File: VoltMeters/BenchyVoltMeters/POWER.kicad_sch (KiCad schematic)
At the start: 25 parts, among them J1 POWER CONN, U10 AP3401, U9 TPS7A94

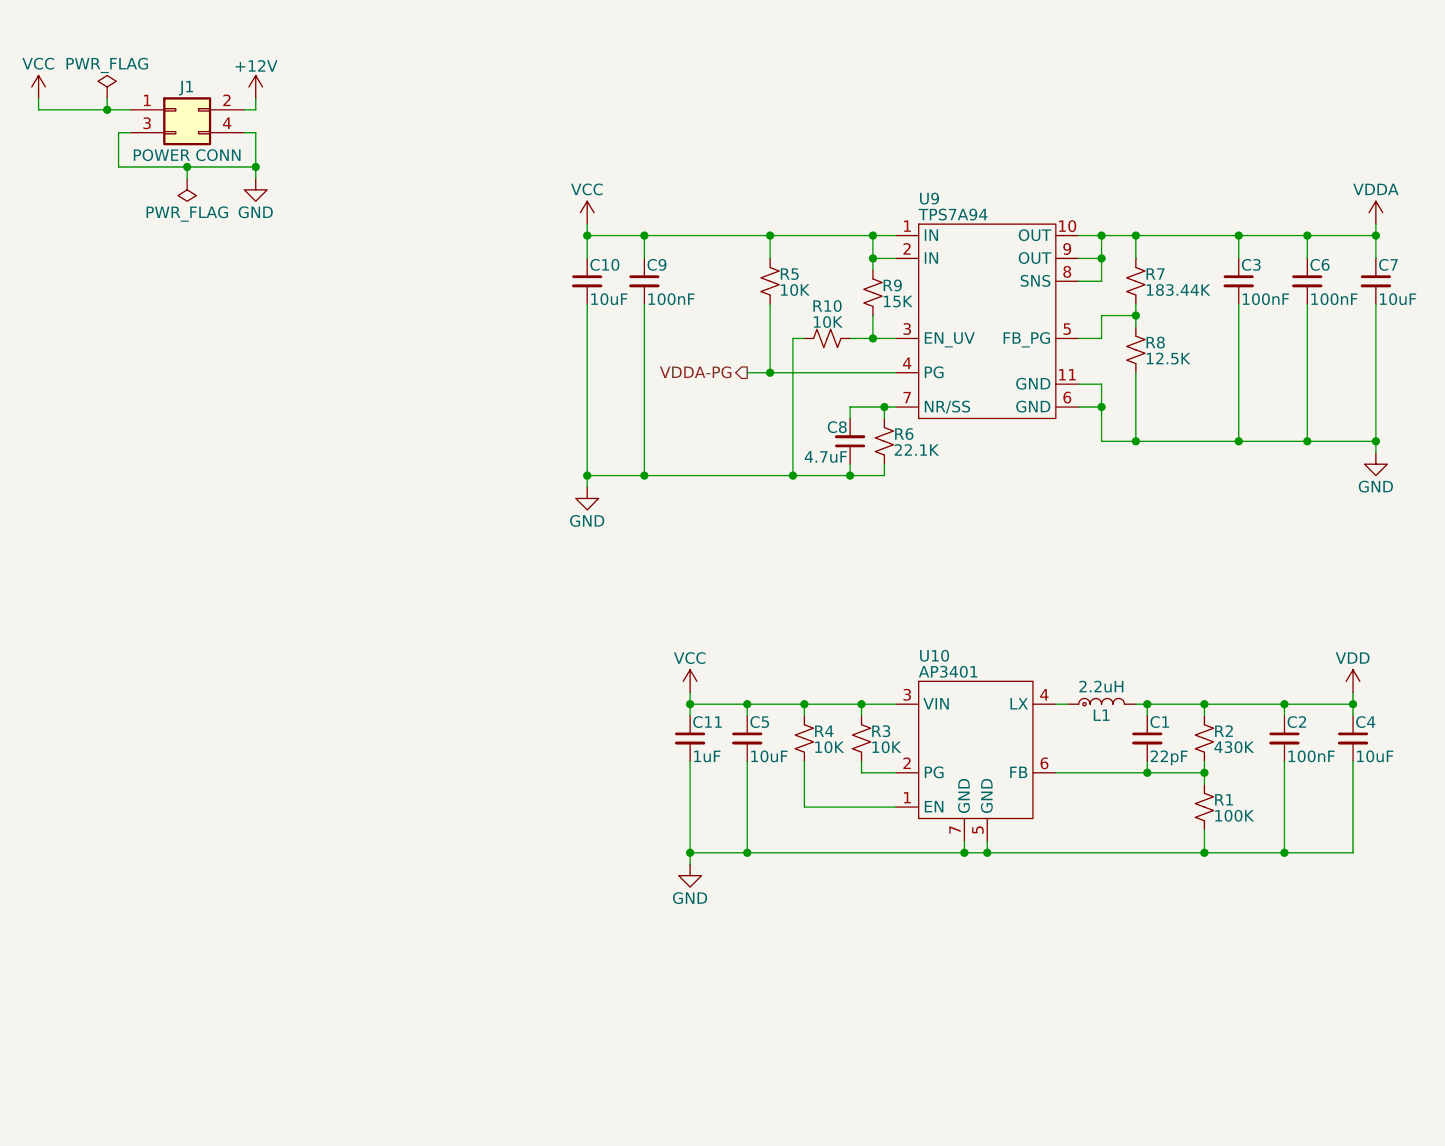
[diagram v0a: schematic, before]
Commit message: Add voltmeter PCB
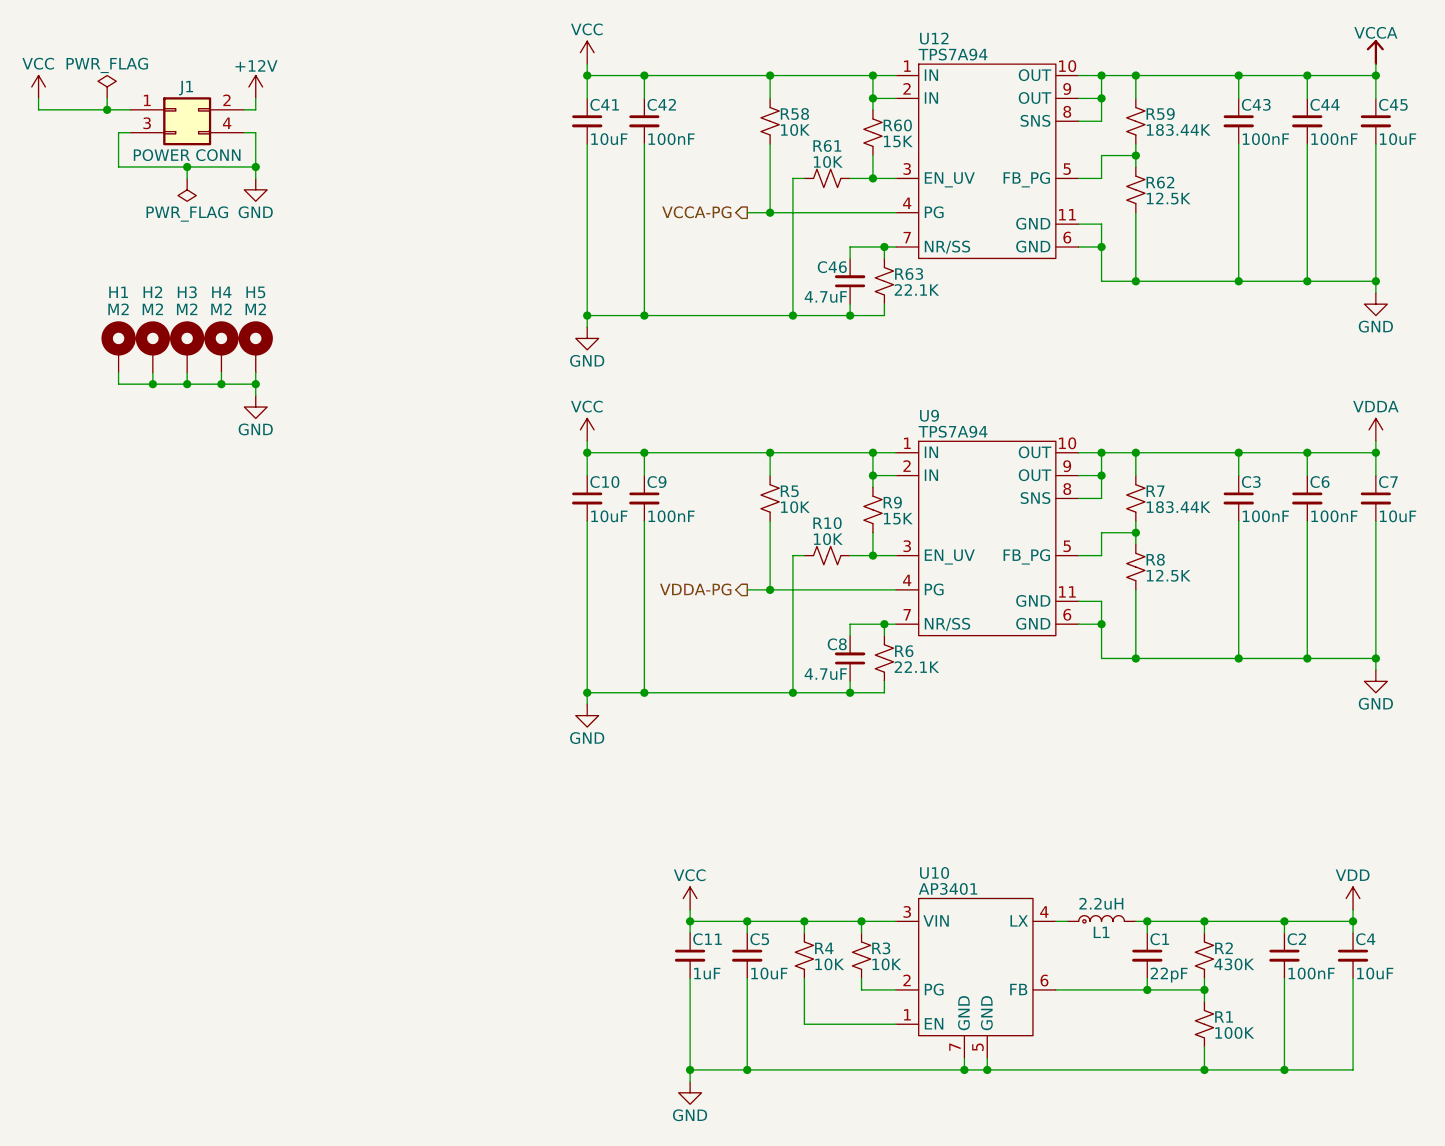
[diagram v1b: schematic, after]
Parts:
- added C41, C45: 10uF, Capacitor_SMD:C_1210_3225Metric, symbol Device:C_Small
- added C42, C43, C44: 100nF, Capacitor_SMD:C_0402_1005Metric, symbol Device:C_Small
- added C46: 4.7uF, Capacitor_SMD:C_0402_1005Metric, symbol Device:C_Small
- added H1, H2, H3, H4, H5: M2, MountingHole:MountingHole_2.2mm_M2_ISO7380_Pad, symbol Mechanical:MountingHole_Pad
- added R58, R61: 10K, Resistor_SMD:R_0402_1005Metric, symbol Device:R_Small_US
- added R59: 183.44K, Resistor_SMD:R_0402_1005Metric, symbol Device:R_Small_US
- added R60: 15K, Resistor_SMD:R_0402_1005Metric, symbol Device:R_Small_US
- added R62: 12.5K, Resistor_SMD:R_0402_1005Metric, symbol Device:R_Small_US
- added R63: 22.1K, Resistor_SMD:R_0402_1005Metric, symbol Device:R_Small_US
- added U12: TPS7A94, Daxxn_Packages:WSON-10-1EP_3x3mm, symbol Daxxn_Regulators:TPS7A94
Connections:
- net GND: now also C41.2, C42.2, C43.2, C44.2, C45.2, C46.1, H1.1, H2.1, H3.1, H4.1, H5.1, R61.1, R62.2, R63.2, U12.11 (GND), U12.6 (GND)
- net VCC: now also C41.1, C42.1, R58.1, R60.1, U12.1 (IN), U12.2 (IN)
- new net: C46.2, R63.1, U12.7 (NR/SS)
- new net: R60.2, R61.2, U12.3 (EN_UV)
- new net: R59.2, R62.1, U12.5 (FB_PG)
- new net VCCA: C43.1, C44.1, C45.1, R59.1, U12.10 (OUT), U12.8 (SNS), U12.9 (OUT)
- new net VCCA-PG: R58.2, U12.4 (PG)
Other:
- moved on the sheet: C1, C10, C11, C2, C3, C4, C5, C6, C7, C8, C9, L1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
